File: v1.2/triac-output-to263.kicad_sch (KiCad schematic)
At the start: 7 parts, among them Q3 T835-600B, Q4 2N7002, U6 TLP160G

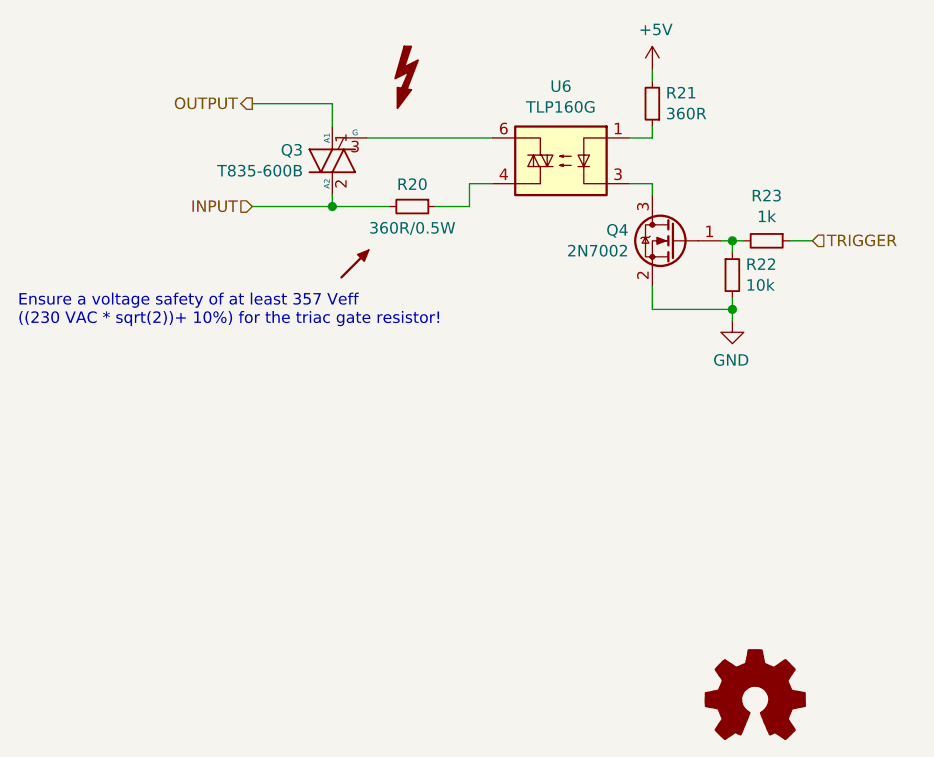
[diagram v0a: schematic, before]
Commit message: change q7 to TO263 (D2PAK) package
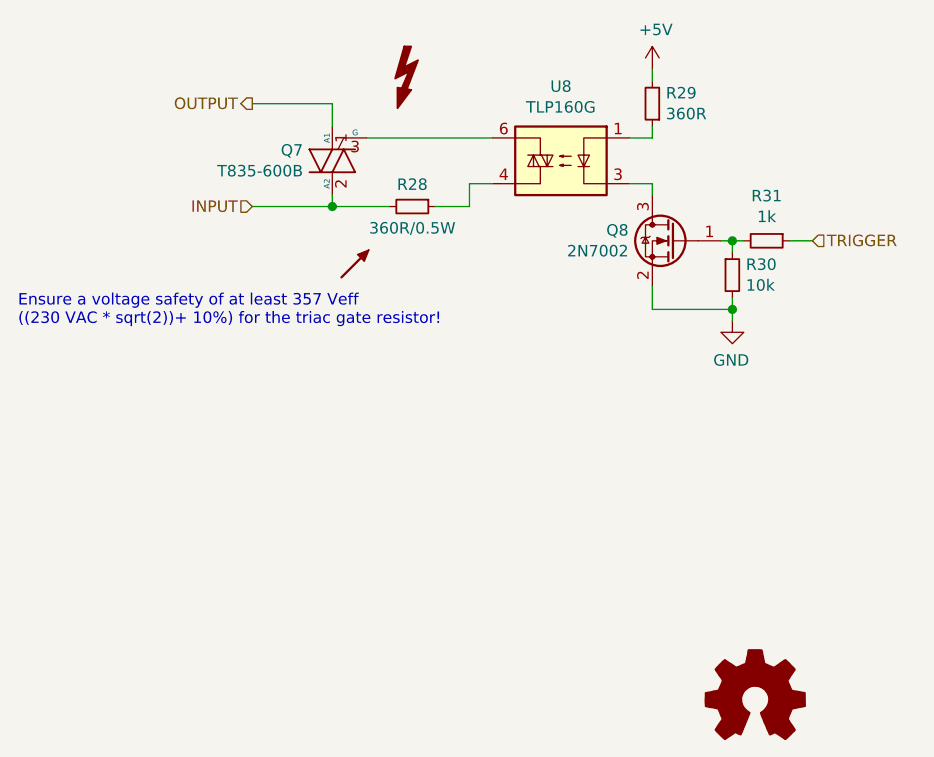
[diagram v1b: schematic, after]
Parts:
- removed Q3: T835-600B, Package_TO_SOT_SMD:TO-252-2, symbol Triac_Thyristor:BT138-600
- removed Q4: 2N7002, Package_TO_SOT_SMD:SOT-23, symbol Transistor_FET:2N7002
- removed R20: 360R/0.5W, Resistor_SMD:R_1206_3216Metric_Pad1.30x1.75mm_HandSolder, symbol Device:R_Small
- removed R21: 360R, Resistor_SMD:R_0603_1608Metric_Pad0.98x0.95mm_HandSolder, symbol Device:R_Small
- removed R22: 10k, Resistor_SMD:R_0603_1608Metric_Pad0.98x0.95mm_HandSolder, symbol Device:R_Small
- removed R23: 1k, Resistor_SMD:R_0603_1608Metric_Pad0.98x0.95mm_HandSolder, symbol Device:R_Small
- removed U6: TLP160G, Package_SO:MFSOP6-4_4.4x3.6mm_P1.27mm, symbol Relay_SolidState:TLP160G
- added Q7: T835-600B, Package_TO_SOT_SMD:TO-263-2, symbol Triac_Thyristor:BT138-600
- added Q8: 2N7002, Package_TO_SOT_SMD:SOT-23, symbol Transistor_FET:2N7002
- added R28: 360R/0.5W, Resistor_SMD:R_1206_3216Metric_Pad1.30x1.75mm_HandSolder, symbol Device:R_Small
- added R29: 360R, Resistor_SMD:R_0603_1608Metric_Pad0.98x0.95mm_HandSolder, symbol Device:R_Small
- added R30: 10k, Resistor_SMD:R_0603_1608Metric_Pad0.98x0.95mm_HandSolder, symbol Device:R_Small
- added R31: 1k, Resistor_SMD:R_0603_1608Metric_Pad0.98x0.95mm_HandSolder, symbol Device:R_Small
- added U8: TLP160G, Package_SO:MFSOP6-4_4.4x3.6mm_P1.27mm, symbol Relay_SolidState:TLP160G
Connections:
- net +5V: now also R29.2
- net GND: now also Q8.2 (S), R30.2
- net INPUT: now also Q7.2 (A2), R28.2
- net OUTPUT: now also Q7.1 (A1)
- net TRIGGER: now also R31.1
- new net: Q7.3 (G), U8.6
- new net: R29.1, U8.1
- new net: Q8.3 (D), U8.3
- new net: R28.1, U8.4
- new net: Q8.1 (G), R30.1, R31.2
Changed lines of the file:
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@@
     (effects (font (size 1.27 1.27)) (justify left))
   )
-  (symbol (lib_id "power:+5V") (at 124.46 41.91 0)
+  (symbol (lib_id "power:+5V") (at 124.46 41.91 0) (unit 1)
     (in_bom yes) (on_board yes)
-    (property "Reference" "#PWR049" (id 0) (at 124.46 45.72 0)
+    (property "Reference" "#PWR0107" (id 0) (at 124.46 45.72 0)
       (effects (font (size 1.27 1.27)) hide)
     )
@@
     )
   )
-  (symbol (lib_id "power:GND") (at 133.35 69.85 0) (mirror y)
+  (symbol (lib_id "power:GND") (at 133.35 69.85 0) (mirror y) (unit 1)
     (in_bom yes) (on_board yes)
-    (property "Reference" "#PWR050" (id 0) (at 133.35 76.2 0)
+    (property "Reference" "#PWR0106" (id 0) (at 133.35 76.2 0)
       (effects (font (size 1.27 1.27)) hide)
     )
@@
     )
   )
-  (symbol (lib_id "Graphic:SYM_Arrow45_Small") (at 91.44 63.5 90)
+  (symbol (lib_id "Graphic:SYM_Arrow45_Small") (at 91.44 63.5 90) (unit 1)
     (in_bom yes) (on_board yes)
-    (property "Reference" "#SYM?" (id 0) (at 90.424 59.182 0)
+    (property "Reference" "#SYM9" (id 0) (at 90.424 59.182 0)
       (effects (font (size 1.27 1.27)) hide)
     )
@@
     )
   )
-  (symbol (lib_id "Device:R_Small") (at 97.79 57.15 270)
+  (symbol (lib_id "Device:R_Small") (at 97.79 57.15 270) (unit 1)
     (in_bom yes) (on_board yes)
-    (property "Reference" "R20" (id 0) (at 97.79 54.7116 90))
+    (property "Reference" "R28" (id 0) (at 97.79 54.7116 90))
     (property "Value" "360R/0.5W" (id 1) (at 97.79 59.563 90))
     (property "Footprint" "Resistor_SMD:R_1206_3216Metric_Pad1.30x1.75mm_HandSolder" (id 2) (at 97.79 57.15 0)
@@
     )
   )
-  (symbol (lib_id "Device:R_Small") (at 124.46 45.72 180)
+  (symbol (lib_id "Device:R_Small") (at 124.46 45.72 180) (unit 1)
     (in_bom yes) (on_board yes)
-    (property "Reference" "R21" (id 0) (at 125.9586 44.5516 0)
+    (property "Reference" "R29" (id 0) (at 125.9586 44.5516 0)
       (effects (font (size 1.27 1.27)) (justify right))
     )
@@
     )
   )
-  (symbol (lib_id "Device:R_Small") (at 133.35 64.77 0)
+  (symbol (lib_id "Device:R_Small") (at 133.35 64.77 0) (unit 1)
     (in_bom yes) (on_board yes)
-    (property "Reference" "R22" (id 0) (at 134.8486 63.6016 0)
+    (property "Reference" "R30" (id 0) (at 134.8486 63.6016 0)
       (effects (font (size 1.27 1.27)) (justify left))
     )
@@
     )
   )
-  (symbol (lib_id "Device:R_Small") (at 137.16 60.96 270)
+  (symbol (lib_id "Device:R_Small") (at 137.16 60.96 270) (unit 1)
     (in_bom yes) (on_board yes)
-    (property "Reference" "R23" (id 0) (at 137.16 55.9816 90))
+    (property "Reference" "R31" (id 0) (at 137.16 55.9816 90))
     (property "Value" "1k" (id 1) (at 137.16 58.293 90))
     (property "Footprint" "Resistor_SMD:R_0603_1608Metric_Pad0.98x0.95mm_HandSolder" (id 2) (at 137.16 60.96 0)
@@
     )
   )
-  (symbol (lib_id "Graphic:SYM_Flash_Small") (at 97.155 43.18 0)
+  (symbol (lib_id "Graphic:SYM_Flash_Small") (at 97.155 43.18 0) (unit 1)
     (in_bom yes) (on_board yes)
-    (property "Reference" "#SYM?" (id 0) (at 94.869 43.18 90)
+    (property "Reference" "#SYM10" (id 0) (at 94.869 43.18 90)
       (effects (font (size 1.27 1.27)) hide)
     )
@@
     )
   )
-  (symbol (lib_id "Triac_Thyristor:BT138-600") (at 88.9 52.07 180)
+  (symbol (lib_id "Triac_Thyristor:BT138-600") (at 88.9 52.07 180) (unit 1)
     (in_bom yes) (on_board yes)
-    (property "Reference" "Q3" (id 0) (at 85.6488 50.9016 0)
+    (property "Reference" "Q7" (id 0) (at 85.6488 50.9016 0)
       (effects (font (size 1.27 1.27)) (justify left))
     )
@@
       (effects (font (size 1.27 1.27)) (justify left))
     )
-    (property "Footprint" "Package_TO_SOT_SMD:TO-252-2" (id 2) (at 83.82 50.165 0)
+    (property "Footprint" "Package_TO_SOT_SMD:TO-263-2" (id 2) (at 83.82 50.165 0)
       (effects (font (size 1.27 1.27) italic) (justify left) hide)
     )
@@
     )
   )
-  (symbol (lib_id "Transistor_FET:2N7002") (at 127 60.96 0) (mirror y)
+  (symbol (lib_id "Transistor_FET:2N7002") (at 127 60.96 0) (mirror y) (unit 1)
     (in_bom yes) (on_board yes)
-    (property "Reference" "Q4" (id 0) (at 121.8184 59.7916 0)
+    (property "Reference" "Q8" (id 0) (at 121.8184 59.7916 0)
       (effects (font (size 1.27 1.27)) (justify left))
     )
@@
     )
   )
-  (symbol (lib_id "Graphic:Logo_Open_Hardware_Small") (at 135.89 112.014 0)
+  (symbol (lib_id "Graphic:Logo_Open_Hardware_Small") (at 135.89 112.014 0) (unit 1)
     (in_bom yes) (on_board yes)
-    (property "Reference" "#LOGO?" (id 0) (at 135.89 105.029 0)
+    (property "Reference" "#LOGO5" (id 0) (at 135.89 105.029 0)
       (effects (font (size 1.27 1.27)) hide)
     )
@@
     )
   )
-  (symbol (lib_id "Relay_SolidState:TLP160G") (at 114.3 52.07 0) (mirror y)
+  (symbol (lib_id "Relay_SolidState:TLP160G") (at 114.3 52.07 0) (mirror y) (unit 1)
     (in_bom yes) (on_board yes)
-    (property "Reference" "U6" (id 0) (at 114.3 43.815 0))
+    (property "Reference" "U8" (id 0) (at 114.3 43.815 0))
     (property "Value" "TLP160G" (id 1) (at 114.3 46.1264 0))
     (property "Footprint" "Package_SO:MFSOP6-4_4.4x3.6mm_P1.27mm" (id 2) (at 114.3 59.69 0)
